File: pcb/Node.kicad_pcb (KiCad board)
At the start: 4 copper layers, 50 x 50 mm, 164 parts, among them J1 LCD, J10 SPI, J11 GPA[0..3], J13 Power In, J14 SERIAL, J2 USB_C_USB2.0_16P, J3 INDICATOR, J4 GPB[0..3], J5 GPB[4..7], J6 BTN[0..3], J7 GPA[4..7], J8 QWIIC1, J9 QWIIC2, Q1 MMBT2222A, SW1 RESET, SW2 BOOT, U1 ESP32-S3-WROOM-1-N8R2, U2 LM66200DRLR, U3 USBLC6-2P6, U4 MCP23017_ML, U6 LM66200DRLR, U7 AZ1084-3.3

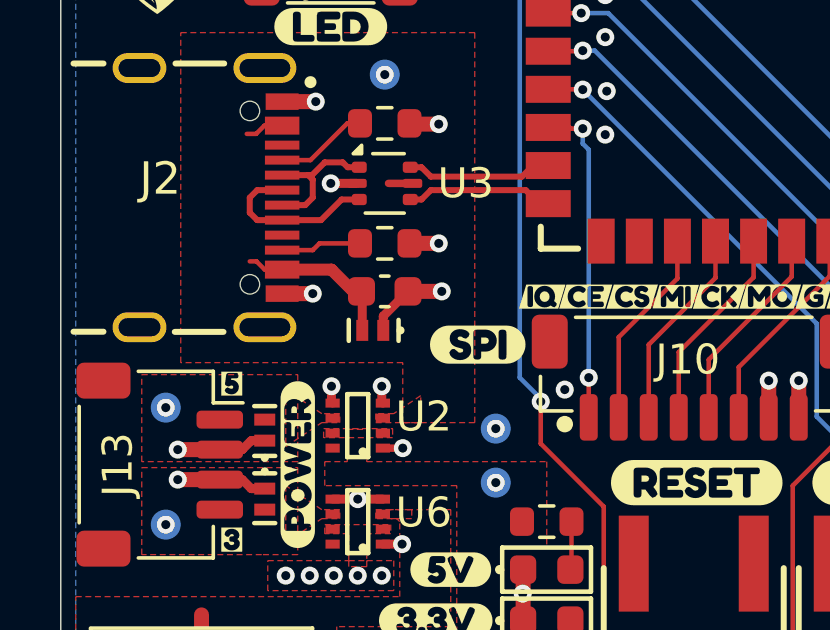
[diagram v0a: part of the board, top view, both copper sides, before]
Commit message: Removed duplicative ESB on USB
Updated descriptions for consistency
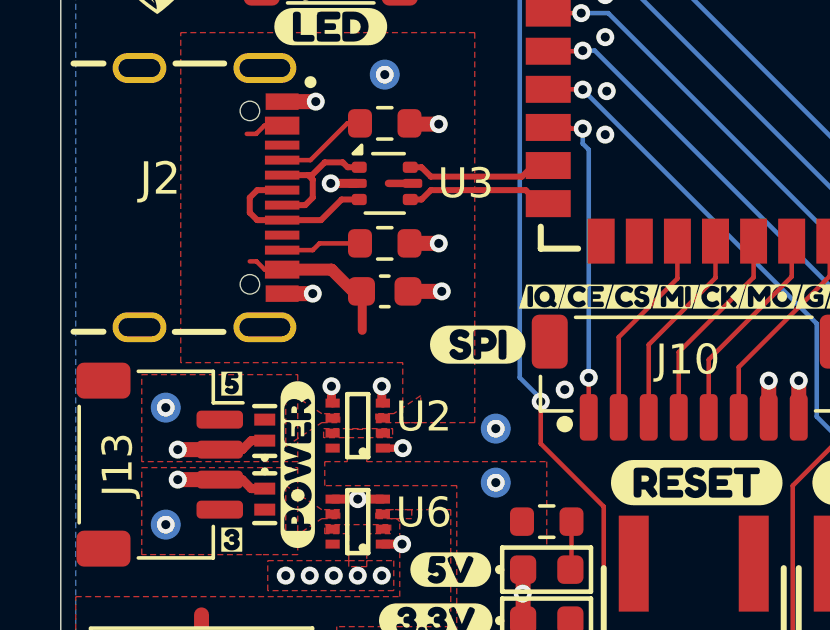
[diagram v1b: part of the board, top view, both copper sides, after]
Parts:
- removed D3: PESD5V5C1BL, CRGM Passive:DFN1006-2
- R15: value 4.7k -> 4.7K
- R16: value 1k -> 1K
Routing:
- net GND: track 91.3 -> 89.6 mm

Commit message: Fixed cap values on reset button
Fixed all part numbers and extended parameters.
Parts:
- C4: value 10uF -> 0.1uF
- LS1: value CMT-0502-75-SMT-TR -> FUET-5025
- U4: value MCP23017_ML -> MCP23017T-E/ML

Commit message: Rationalized attributes; excluded some footprints from BOM
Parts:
- LOGO3: value Logo_Open_Hardware_Small -> ~
- TP5: value ~ -> IO1
- TP6: value ~ -> IO2
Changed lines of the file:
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@@
 			)
 		)
-		(property "Value" "~"
+		(property "Value" "IO2"
 			(at 0 1.55 0)
 			(layer "F.Fab")
@@
 		(sheetname "/MCU/")
 		(sheetfile "mcu.kicad_sch")
-		(attr exclude_from_pos_files)
+		(attr exclude_from_pos_files exclude_from_bom)
 		(fp_circle
 			(center 0 0)
@@
 		(sheetname "/MCU/")
 		(sheetfile "mcu.kicad_sch")
-		(attr exclude_from_pos_files)
+		(attr exclude_from_pos_files exclude_from_bom)
 		(fp_circle
 			(center 0 0)
@@
 			)
 		)
-		(property "Value" "~"
+		(property "Value" "IO1"
 			(at 0 1.55 0)
 			(layer "F.Fab")
@@
 		(sheetname "/MCU/")
 		(sheetfile "mcu.kicad_sch")
-		(attr exclude_from_pos_files)
+		(attr exclude_from_pos_files exclude_from_bom)
 		(fp_circle
 			(center 0 0)
@@
 		(sheetname "/Requirements/")
 		(sheetfile "requirements.kicad_sch")
+		(attr exclude_from_bom)
 		(fp_poly
 			(pts
@@
 		(sheetname "/Requirements/")
 		(sheetfile "requirements.kicad_sch")
+		(attr exclude_from_bom)
 		(fp_poly
 			(pts
@@
 		(sheetname "/Power/")
 		(sheetfile "power.kicad_sch")
-		(attr exclude_from_pos_files)
+		(attr exclude_from_pos_files exclude_from_bom)
 		(fp_circle
 			(center 0 0)
@@
 		(sheetname "/MCU/")
 		(sheetfile "mcu.kicad_sch")
-		(attr exclude_from_pos_files)
+		(attr exclude_from_pos_files exclude_from_bom)
 		(fp_circle
 			(center 0 0)
@@
 		(sheetname "/Requirements/")
 		(sheetfile "requirements.kicad_sch")
+		(attr exclude_from_bom)
 		(fp_poly
 			(pts
@@
 		(sheetname "/MCU/")
 		(sheetfile "mcu.kicad_sch")
-		(attr exclude_from_pos_files)
+		(attr exclude_from_pos_files exclude_from_bom)
 		(fp_circle
 			(center 0 0)
@@
 			)
 		)
-		(property "Value" "Logo_Open_Hardware_Small"
+		(property "Value" "~"
 			(at 0.75 0 0)
 			(layer "B.Fab")
@@
 			)
 		)
-		(property "Digikey PN" ""
-			(at 0 0 0)
-			(unlocked yes)
-			(layer "B.Fab")
-			(hide yes)
-			(effects
-				(font
-					(size 1 1)
-					(thickness 0.15)
-				)
-				(justify mirror)
-			)
-		)
-		(property "JLCPCB" ""
+		(property "LCSC" ""
 			(at 0 0 0)
 			(unlocked yes)
@@
 			)
 		)
-		(property "JLCPCB Datasheet" ""
+		(property "Digikey" ""
 			(at 0 0 0)
 			(unlocked yes)
@@
 			)
 		)
-		(property "Mouser PN" ""
+		(property "Mouser" ""
 			(at 0 0 0)
 			(unlocked yes)
@@
 		(sheetname "/MCU/")
 		(sheetfile "mcu.kicad_sch")
-		(attr exclude_from_pos_files)
+		(attr exclude_from_pos_files exclude_from_bom)
 		(fp_circle
 			(center 0 0)
@@
 			)
 		)
-		(property "Digikey PN" ""
-			(at 0 0 180)
-			(unlocked yes)
-			(layer "B.Fab")
-			(hide yes)
-			(effects
-				(font
-					(size 1 1)
-					(thickness 0.15)
-				)
-				(justify mirror)
-			)
-		)
-		(property "JLCPCB" ""
+		(property "LCSC" ""
 			(at 0 0 180)
 			(unlocked yes)
@@
 			)
 		)
-		(property "JLCPCB Datasheet" ""
+		(property "Digikey" ""
 			(at 0 0 180)
 			(unlocked yes)
@@
 			)
 		)
-		(property "Mouser PN" ""
+		(property "Mouser" ""
 			(at 0 0 180)
 			(unlocked yes)
@@
 		(sheetname "/Power/")
 		(sheetfile "power.kicad_sch")
-		(attr exclude_from_pos_files)
+		(attr exclude_from_pos_files exclude_from_bom)
 		(fp_circle
 			(center 0 0)
@@
 		(sheetname "/Power/")
 		(sheetfile "power.kicad_sch")
-		(attr exclude_from_pos_files)
+		(attr exclude_from_pos_files exclude_from_bom)
 		(fp_circle
 			(center 0 0)

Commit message: Continued rationalizing parts
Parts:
- D23: value Orange -> Blue

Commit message: Updated dimensions; updated mounting hole footprint
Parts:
- D23: value Blue -> Orange
- H1, H2, H3, H4: footprint MountingHole:MountingHole_3.2mm_M3_Pad_Via -> CRGM Mechanical:MountingHole_3.2mm_M3_Pad_Via
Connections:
- H1 pad 1: unconnected-(H1-Pad1)_4 -> (no net)
- H2 pad 1: unconnected-(H2-Pad1)_1 -> (no net)
- H3 pad 1: unconnected-(H3-Pad1)_2 -> (no net)
- H4 pad 1: unconnected-(H4-Pad1)_3 -> (no net)
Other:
- board text removed: "Top Layer Horizontal Bottom Layer Vertical"

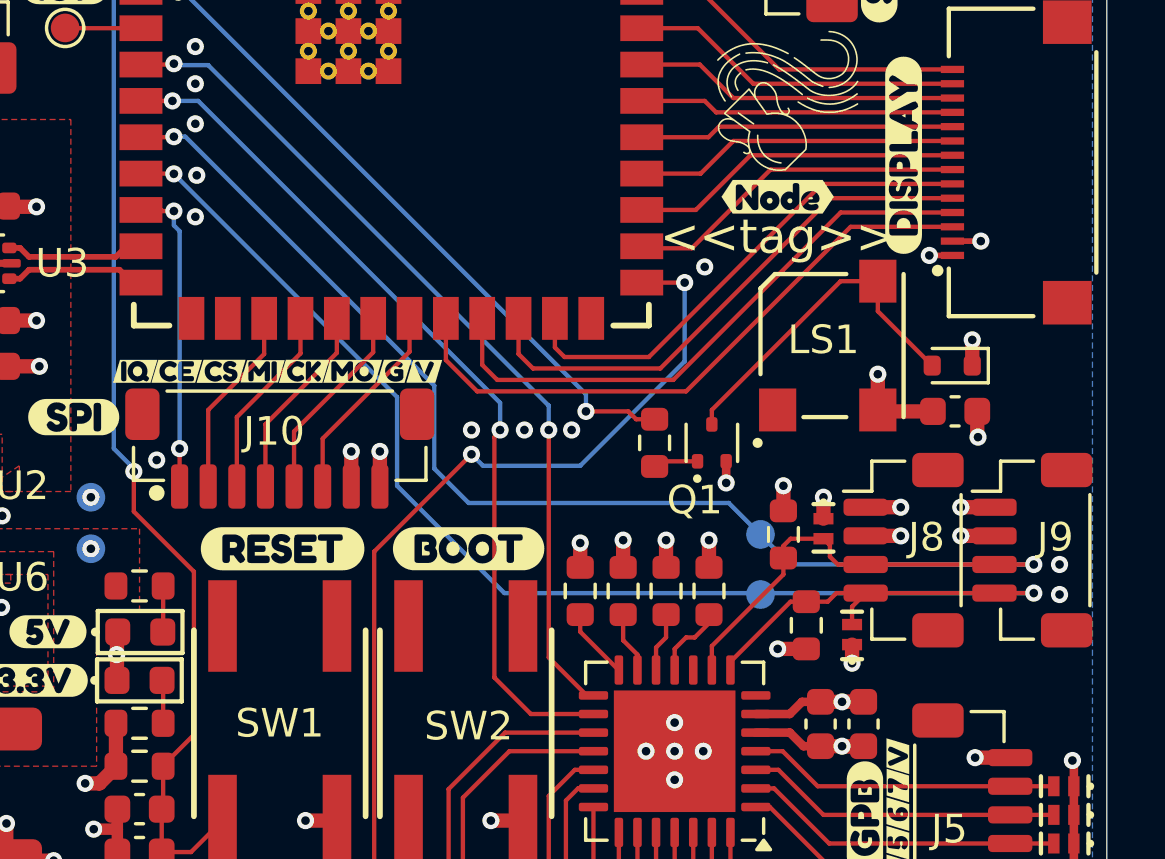
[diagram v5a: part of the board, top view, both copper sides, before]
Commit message: Adjusted part values
Fixed LCSC footprints for connectors
Moved EN 5% instead of 1%
Moved I2C pull ups to 4.7K
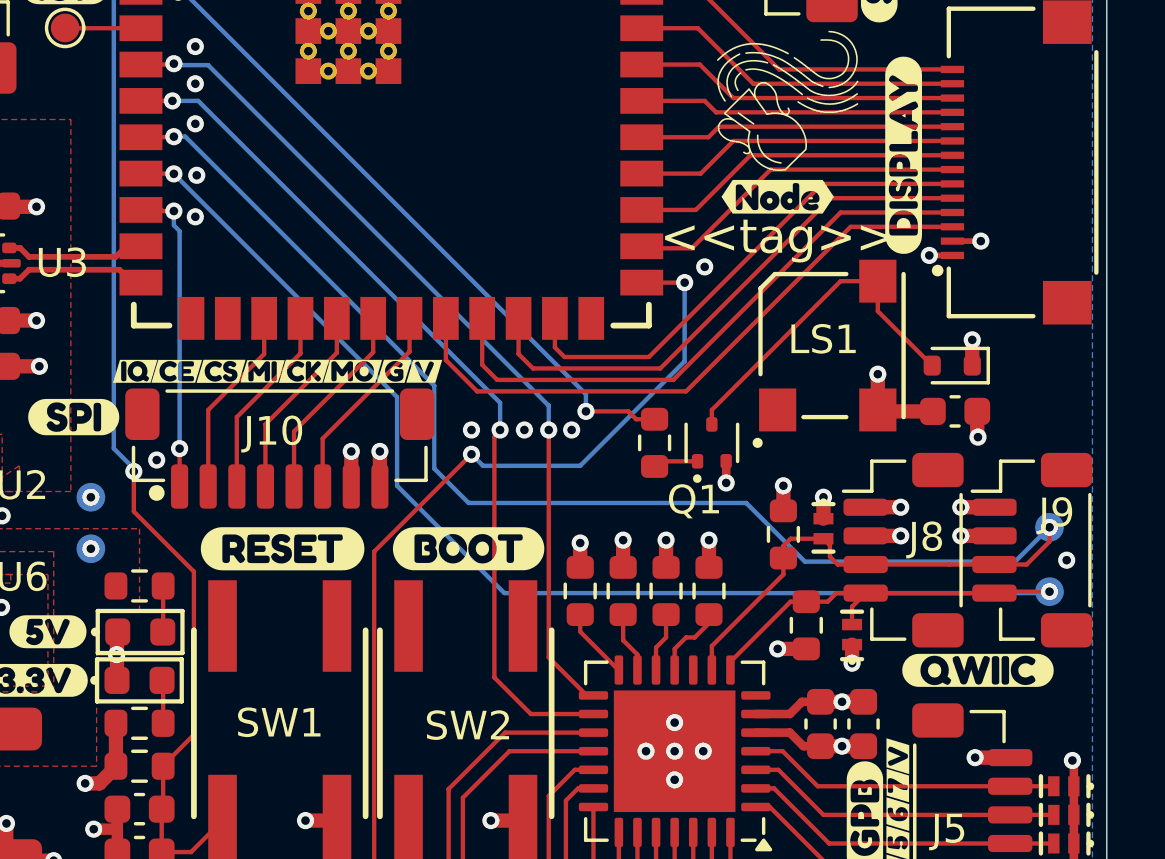
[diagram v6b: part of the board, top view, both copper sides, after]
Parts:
- added kibuzzard-6857318D: G***, kibuzzard-6857318D, F.Cu at (105.5, 81.8)
- R1, R2: value 10K -> 4.7K
- R3: value 10K (1%) -> 10K
- moved TP1 10.1 mm to (108.0, 76.8)
- moved TP2 10.1 mm to (108.0, 79.0)
- moved LOGO3 7.09 mm to (98.5, 58.9)
- moved LOGO1 7.09 mm to (90.7, 63.4)
- moved kibuzzard-67B9F9CD 6.98 mm to (107.5, 80.5)
- moved kibuzzard-67B9F9C2 6.74 mm to (107.3, 75.2)
- moved LOGO2 1.03 mm to (83.3, 73.0)
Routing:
- net I2C_SDA: track 53.9 -> 56.3 mm
- net I2C_SCL: track 52.3 -> 53.4 mm
- net GND: vias 75 -> 74

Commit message: Cleaned up fab layer. Minor tweaks. Updated renders.
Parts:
- removed kibuzzard-680D01D7: G***, kibuzzard-680D01D7
- removed kibuzzard-681035B7: G***, kibuzzard-681035B7
- removed the kibuzzard-68194F3F at (96.0, 55.2)
- removed kibuzzard-683921A3: G***, kibuzzard-683921A3
- removed kibuzzard-683921A8: G***, kibuzzard-683921A8
- removed kibuzzard-683B54F2: G***, kibuzzard-683B54F2
- removed kibuzzard-683B54FF: G***, kibuzzard-683B54FF
- removed kibuzzard-683B5656: G***, kibuzzard-683B5656
- removed kibuzzard-683B5CE2: G***, kibuzzard-683B5CE2
- removed kibuzzard-683B5CED: G***, kibuzzard-683B5CED
- added kibuzzard-68574A7C: G***, kibuzzard-68574A7C, F.Cu at (96.3, 57.2)
- added kibuzzard-68574A8F: G***, kibuzzard-68574A8F, F.Cu at (96.0, 56.2)
- added kibuzzard-68574A9F: G***, kibuzzard-68574A9F, F.Cu at (96.0, 55.2)
- added kibuzzard-68574AC2: G***, kibuzzard-68574AC2, F.Cu at (73.0, 80.4)
- added kibuzzard-68574AD3: G***, kibuzzard-68574AD3, F.Cu at (72.5, 82.1)
- added kibuzzard-68574B95: G***, kibuzzard-68574B95, F.Cu at (73.9, 72.9)
- added kibuzzard-68574D75: G***, kibuzzard-68574D75, B.Cu at (66.0, 75.0)
- added kibuzzard-68574D7F: G***, kibuzzard-68574D7F, B.Cu at (66.4, 78.9)
- added kibuzzard-68574D8A: G***, kibuzzard-68574D8A, B.Cu at (77.3, 75.7)
- added kibuzzard-68574D94: G***, kibuzzard-68574D94, B.Cu at (76.8, 77.6)
- moved kibuzzard-67B9F9CD 0.15 mm to (107.5, 80.6)
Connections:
- J14 pad 1: GND -> TX
- J14 pad 2: TX -> RX
- J14 pad 3: RX -> GND
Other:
- board text added: "x 4"

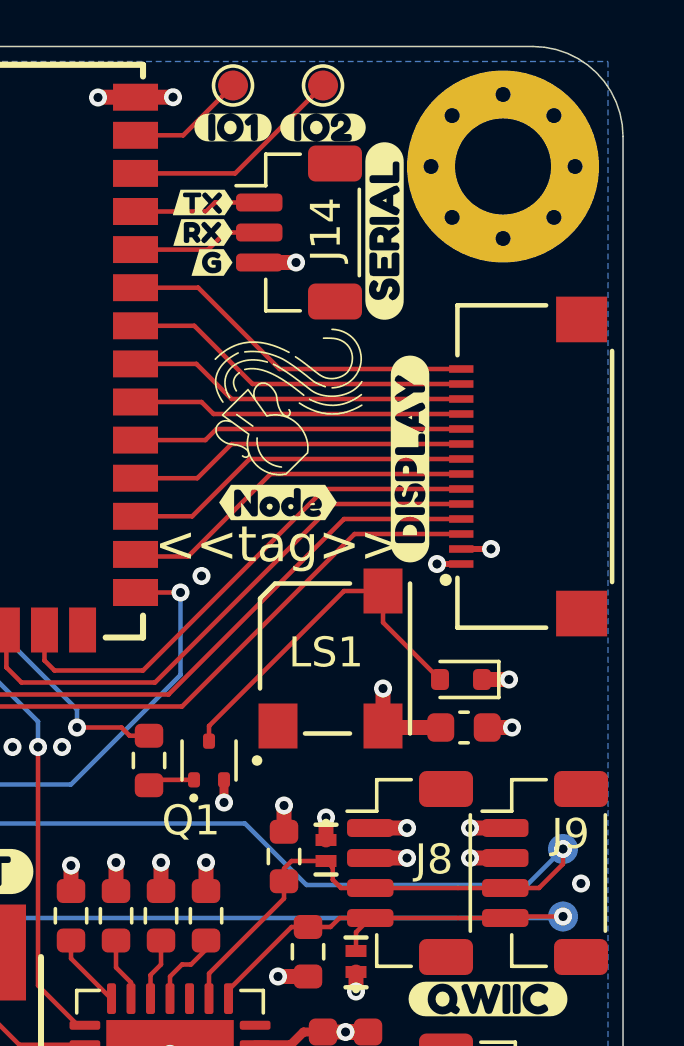
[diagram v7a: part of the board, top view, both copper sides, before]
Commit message: closed #3 and #1
Fixed resistors and values
Widened panel
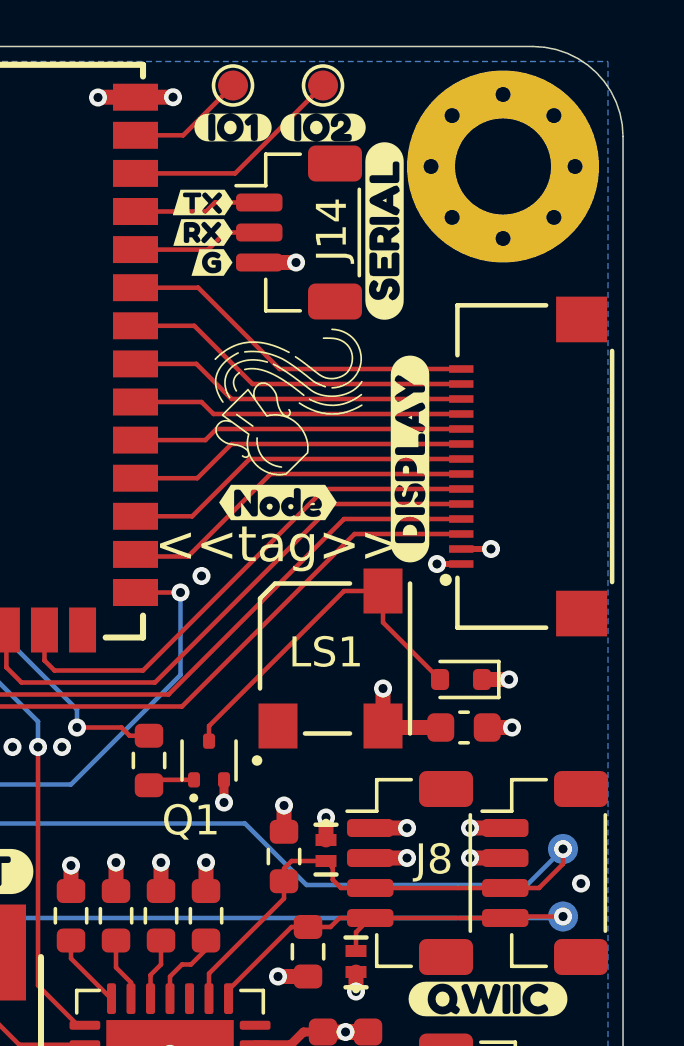
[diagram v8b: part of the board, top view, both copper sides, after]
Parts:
- J1: value LCD -> XF2M-1415-1A
- J10: value SPI -> BM08B-SRSS-TB
- J11: value GPA[0..3] -> BM04B-SRSS-TB
- J13: value Power In -> SM04B-SRSS-TB
- J14: value SERIAL -> BM03B-SRSS-TB; footprint Connector_JST:JST_SH_BM03B-SRSS-TB_1x03-1MP_P1.00mm_Vertical -> CRGM Connector:JST_SH_BM03B-SRSS-TB_1x03-1MP_P1.00mm_Vertical
- J3: value INDICATOR -> BM03B-SRSS-TB
- J4: value GPB[0..3] -> BM06B-SRSS-TB
- J5: value GPB[4..7] -> BM06B-SRSS-TB
- J6: value BTN[0..3] -> BM04B-SRSS-TB
- J7: value GPA[4..7] -> BM06B-SRSS-TB
- J8: value QWIIC1 -> BM04B-SRSS-TB
- J9: value QWIIC2 -> BM04B-SRSS-TB
- SW1: value RESET -> EVQ-Q2B02W
- SW2: value BOOT -> EVQ-Q2B02W
- TP1: value I2C_SDA -> TP
- TP10: value LV5 -> TP
- TP11: value LV33 -> TP
- TP12: value V5 -> TP; footprint TestPoint:TestPoint_Pad_D1.0mm -> CRGM Mechanical:TestPoint_Pad_D1.0mm
- TP2: value I2C_SCL -> TP
- TP3: value OBLO -> TP
- TP4: value USB_5V -> TP
- TP5: value IO1 -> TP
- TP6: value IO2 -> TP
- TP7: value IO7 -> TP
- TP8: value V33 -> TP; footprint TestPoint:TestPoint_Pad_D1.0mm -> CRGM Mechanical:TestPoint_Pad_D1.0mm
- TP9: value LDO_V33 -> TP; footprint TestPoint:TestPoint_Pad_D1.0mm -> CRGM Mechanical:TestPoint_Pad_D1.0mm
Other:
- board text added: "Antenna"
